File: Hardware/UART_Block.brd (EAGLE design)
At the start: 30.5 x 44.5 mm, 29 parts, among them U4 TPS62065

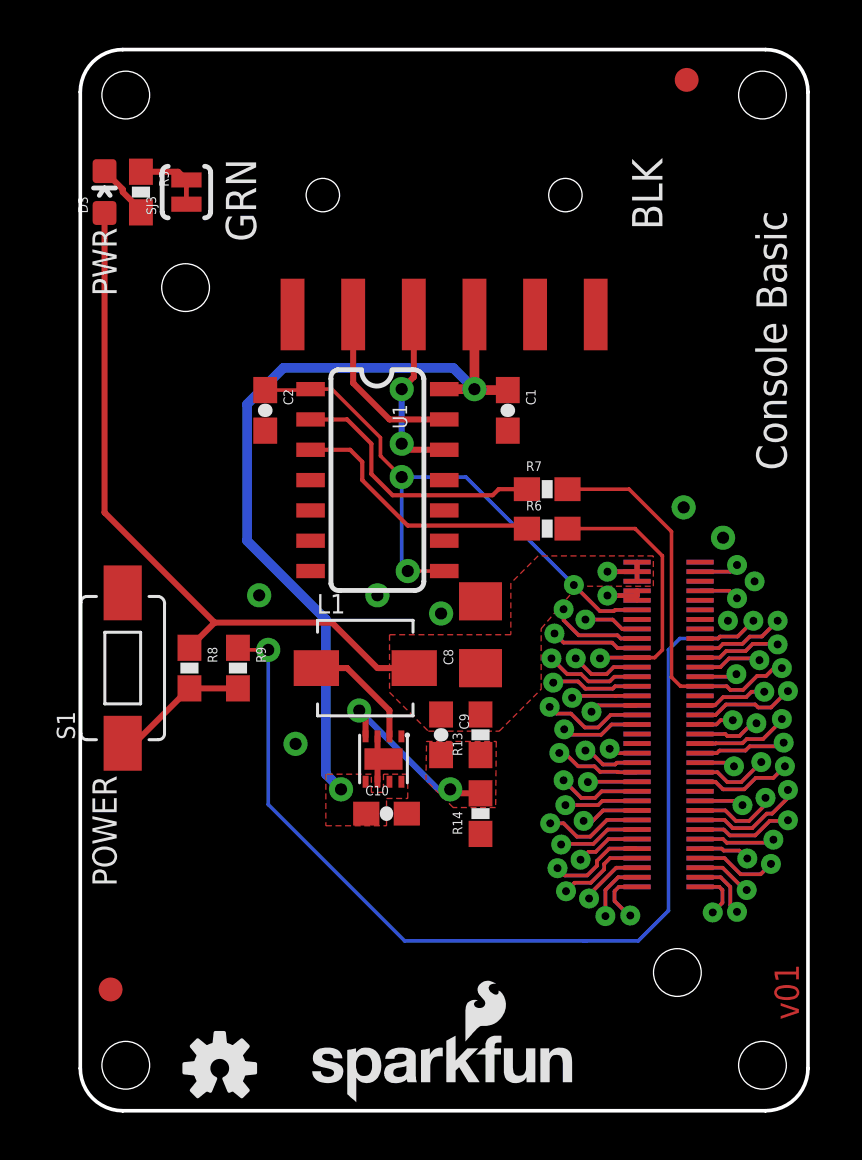
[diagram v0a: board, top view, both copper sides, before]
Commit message: added DCIN pin added DCIN enable circuit corrected Copper pours corrected name changed names of board and SCH replaced power button updated header footprint added units and cleaned up dimensions
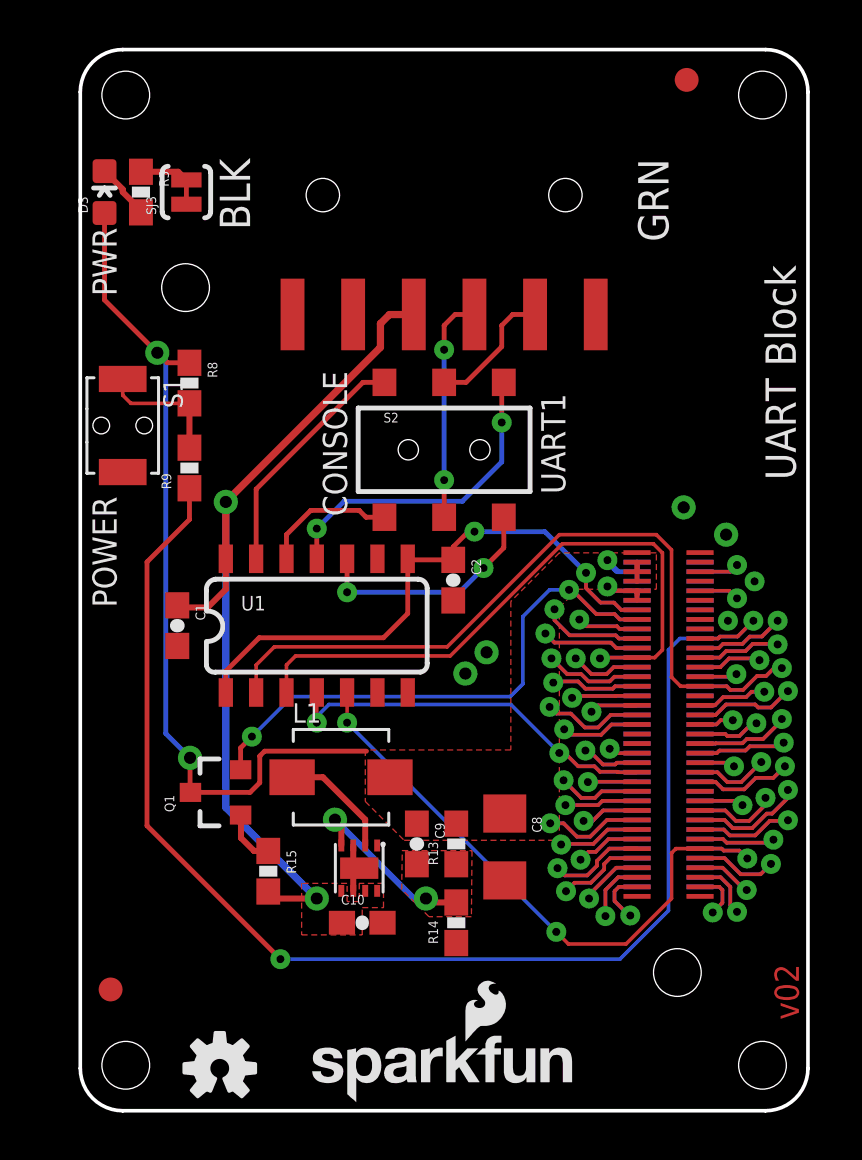
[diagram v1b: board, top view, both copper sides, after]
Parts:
- removed R6, R7: 100, SparkFun-Resistors:0603-RES
- added Q1: BSS138, SparkFun-DiscreteSemi:SOT23-3
- added R15: 1K, SparkFun-Resistors:0603-RES
- added S2: DPDT, SparkFun-Electromechanical:AYZ0202
- S1: device SparkFun-Electromechanical:TACTILE-SWITCH-1101NE -> SparkFun-Electromechanical:TACTILE_SWITCH-SMD-RIGHT-ANGLE
- moved C1 16.5 mm to (4.06, 20.3)
- moved R8 11.9 mm to (4.57, 30.5)
- moved C2 10.6 mm to (15.6, 22.2)
- moved S1 10.2 mm to (1.78, 28.7), turned to 270 degrees
- moved C8 8.95 mm to (17.8, 11.0), turned to 270 degrees
- moved R9 8.62 mm to (4.57, 26.9), turned to 90 degrees
- moved U1 6.60 mm to (9.91, 20.3), turned to 0 degrees
- moved L1 4.68 mm to (10.9, 14.0)
- moved C10 4.68 mm to (11.8, 7.87)
- moved R14 4.68 mm to (15.7, 7.87)
- moved C9 4.68 mm to (14.1, 11.2)
- moved R13 4.68 mm to (15.7, 11.2)
- moved U4 4.68 mm to (11.7, 10.2)
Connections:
- removed net N$3: R7.1, U1.2
- removed net N$4: R6.1, U1.3
- new net DCIN: E1.14, Q1.2, U$3.14
- new net N$1: Q1.1, R15.1
- new net UART1RX: S2.6, U1.10
- new net UART1TX: S2.3, U1.11
- new net UART2RX: S2.4, U1.12
- new net UART2TX: S2.1, U1.13
- net GND: now also JP2.5, JP2.6, S1.2; no longer JP2.1, JP2.2, S1.P$2
- net GP130_UART_1_RX: now also U1.5
- net GP131_UART_1_TX: now also U1.4
- net GP134_UART_2_RX: now also U1.3; no longer R6.2
- net GP135_UART_2_TX: now also U1.2; no longer R7.2
- net N$15: now also S1.1; no longer S1.P$1
- net RXD: now also JP2.2, S2.2; no longer JP2.5, U1.13
- net TXD: now also JP2.3, S2.5; no longer JP2.4, U1.12
- net VCC: now also JP2.4, R15.2; no longer JP2.3
- net VSYS: now also Q1.3
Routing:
- net DCIN: track 0.00 -> 25.8 mm, vias 0 -> 2
- net GP130_UART_1_RX: track 4.30 -> 27.0 mm, vias 1 -> 3
- net GP135_UART_2_TX: track 20.3 -> 35.5 mm
- net GP134_UART_2_RX: track 12.7 -> 27.6 mm
- net UART1TX: track 0.00 -> 13.5 mm, vias 0 -> 2
- net GP131_UART_1_TX: track 7.18 -> 19.9 mm, vias 1 -> 2
- net PWRBTN#: track 45.0 -> 57.4 mm
- net N$3: track 11.2 -> 0.00 mm
- net N$4: track 10.9 -> 0.00 mm
- net UART2TX: track 0.00 -> 10.1 mm
- net UART1RX: track 0.00 -> 10.0 mm, vias 0 -> 2
- net UART2RX: track 0.00 -> 5.65 mm
- net VSYS: track 34.2 -> 39.5 mm, vias 1 -> 3
- net VCC: track 34.3 -> 38.1 mm
- net N$1: track 0.00 -> 2.33 mm
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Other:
- board text added: "CONSOLE"
- board text added: "NOTE: Units are in Inches"
- board text added: "UART Block"
- board text added: "UART1"
- board text added: "v02"
- board text removed: "Connectors Go Here"
- board text removed: "Console Basic"
- board text removed: "LED's and selector switches go here"
- board text removed: "Max Board Length"
- board text removed: "Nothing goes here... I mean it."
- board text removed: "v01"

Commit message: Rev to 10, fix gnd, pwr, txt
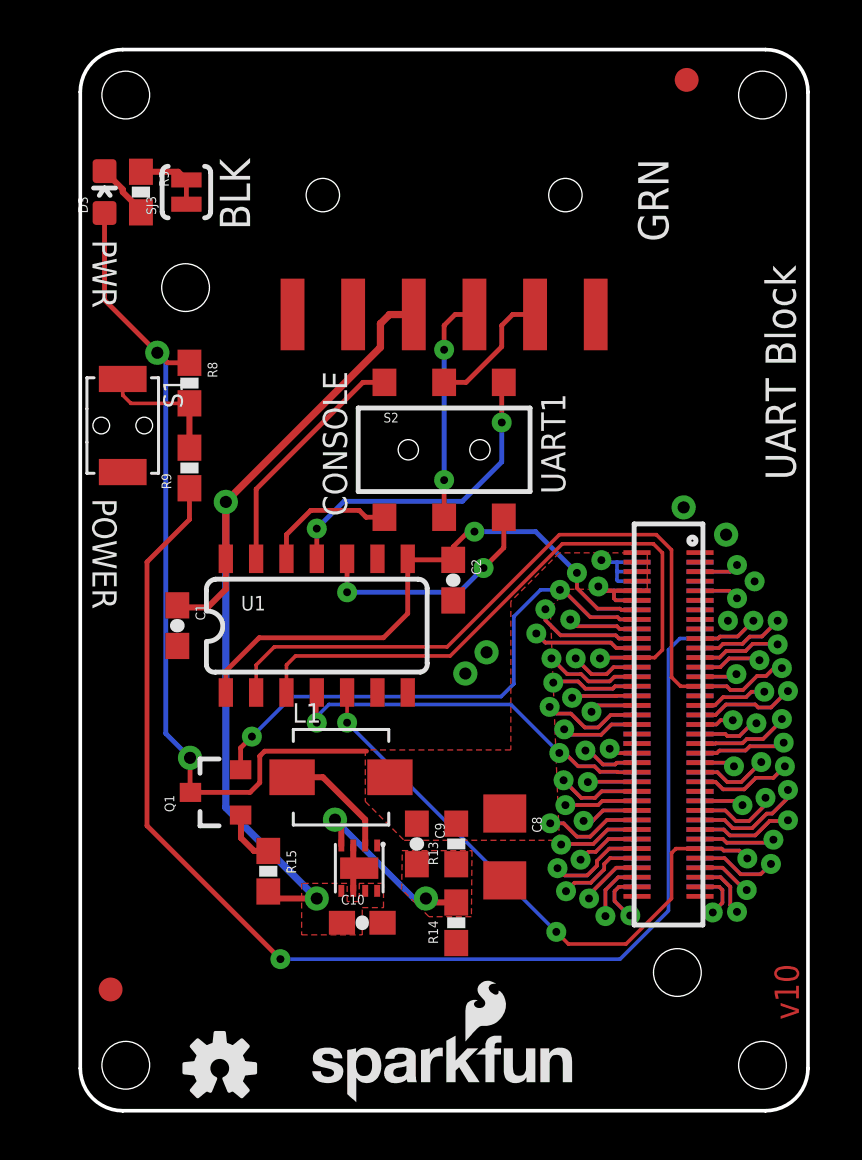
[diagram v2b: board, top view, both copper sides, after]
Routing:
- net 3.3V: track 3.63 -> 6.03 mm
- net USB_VBUS: track 8.18 -> 8.94 mm
- net USB_DN: track 8.47 -> 9.23 mm
- net USB_DP: track 5.16 -> 5.92 mm
- net VSYS: track 39.5 -> 40.0 mm
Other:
- board text added: "v10"
- board text removed: "v02"

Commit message: Fix packages, silk, filter cap.
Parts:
- C9: value 9.0pF -> 47pF
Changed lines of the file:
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@@
 <layer number="2" name="Route2" color="1" fill="3" visible="no" active="yes"/>
 <layer number="15" name="Route15" color="4" fill="6" visible="no" active="yes"/>
-<layer number="16" name="Bottom" color="1" fill="1" visible="yes" active="yes"/>
+<layer number="16" name="Bottom" color="1" fill="1" visible="no" active="yes"/>
 <layer number="17" name="Pads" color="2" fill="1" visible="yes" active="yes"/>
 <layer number="18" name="Vias" color="2" fill="1" visible="yes" active="yes"/>
@@
 <layer number="20" name="Dimension" color="15" fill="1" visible="yes" active="yes"/>
 <layer number="21" name="tPlace" color="16" fill="1" visible="yes" active="yes"/>
-<layer number="22" name="bPlace" color="14" fill="1" visible="yes" active="yes"/>
+<layer number="22" name="bPlace" color="14" fill="1" visible="no" active="yes"/>
 <layer number="23" name="tOrigins" color="15" fill="1" visible="yes" active="yes"/>
-<layer number="24" name="bOrigins" color="15" fill="1" visible="yes" active="yes"/>
+<layer number="24" name="bOrigins" color="15" fill="1" visible="no" active="yes"/>
 <layer number="25" name="tNames" color="7" fill="1" visible="no" active="yes"/>
 <layer number="26" name="bNames" color="7" fill="1" visible="no" active="yes"/>
@@
 <layer number="43" name="vRestrict" color="2" fill="10" visible="no" active="yes"/>
 <layer number="44" name="Drills" color="7" fill="1" visible="no" active="yes"/>
-<layer number="45" name="Holes" color="7" fill="1" visible="yes" active="yes"/>
+<layer number="45" name="Holes" color="7" fill="1" visible="no" active="yes"/>
 <layer number="46" name="Milling" color="3" fill="1" visible="no" active="yes"/>
-<layer number="51" name="tDocu" color="6" fill="1" visible="yes" active="yes"/>
+<layer number="51" name="tDocu" color="6" fill="1" visible="no" active="yes"/>
 <layer number="3" name="Route3" color="4" fill="3" visible="no" active="no"/>
 <layer number="4" name="Route4" color="1" fill="4" visible="no" active="no"/>
@@
 <text x="10.668" y="27.94" size="1.016" layer="21" font="vector" ratio="15" rot="R90" align="center">CONSOLE</text>
 <text x="19.812" y="27.94" size="1.016" layer="21" font="vector" ratio="15" rot="R90" align="center">UART1</text>
+<wire x1="12.192" y1="9.525" x2="12.192" y2="8.89" width="0.1524" layer="41"/>
 </plain>
 <attributes>
@@
 <element name="R13" library="SparkFun-Resistors" package="0603-RES" value="680k" x="15.748" y="11.176" rot="R90"/>
 <element name="R14" library="SparkFun-Resistors" package="0603-RES" value="120k" x="15.748" y="7.874" rot="R90"/>
-<element name="C9" library="SparkFun-Capacitors" package="0603-CAP" value="9.0pF" x="14.097" y="11.176" rot="R270">
-<attribute name="PROD_ID" value="CAP-09341" x="10.668" y="27.178" size="1.778" layer="27" rot="R270" display="off"/>
+<element name="C9" library="SparkFun-Capacitors" package="0603-CAP" value="47pF" x="14.097" y="11.176" rot="R270">
+<attribute name="PROD_ID" value="CAP-08913" x="10.668" y="27.178" size="1.778" layer="27" rot="R270" display="off"/>
 </element>
 <element name="C10" library="SparkFun-Capacitors" package="0603-CAP" value="4.7uF" x="11.811" y="7.874">

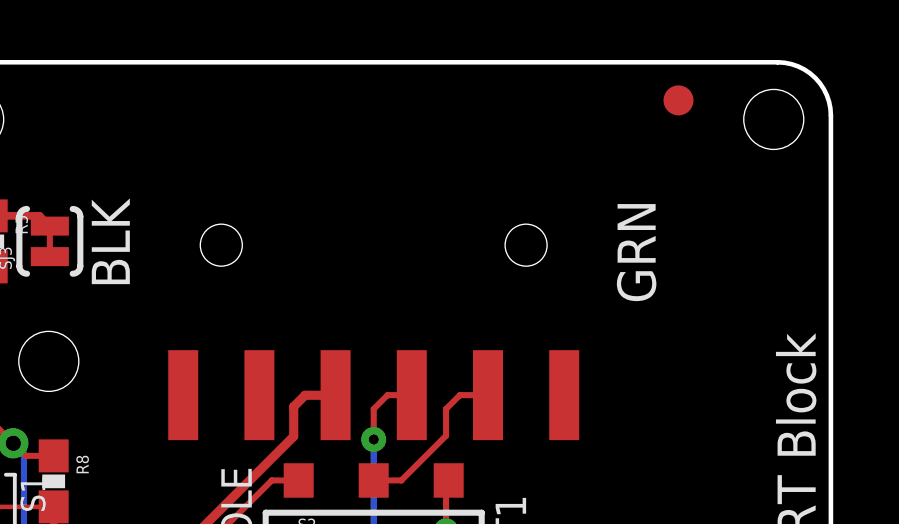
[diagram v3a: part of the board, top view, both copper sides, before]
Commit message: Ready for reds Updated and corrected some labels on UART connector. No signal changes. No known to-do items
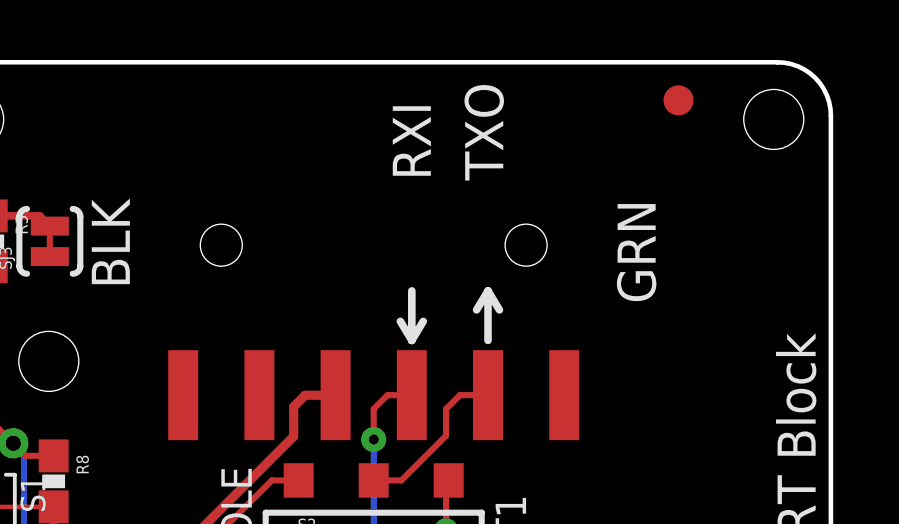
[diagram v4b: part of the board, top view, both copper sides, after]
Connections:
- net RXD renamed TXO
- net TXD renamed RXI
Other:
- board text added: "RXI"
- board text added: "TXO"
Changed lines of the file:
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@@
 <layer number="2" name="Route2" color="1" fill="3" visible="no" active="yes"/>
 <layer number="15" name="Route15" color="4" fill="6" visible="no" active="yes"/>
-<layer number="16" name="Bottom" color="1" fill="1" visible="no" active="yes"/>
+<layer number="16" name="Bottom" color="1" fill="1" visible="yes" active="yes"/>
 <layer number="17" name="Pads" color="2" fill="1" visible="yes" active="yes"/>
 <layer number="18" name="Vias" color="2" fill="1" visible="yes" active="yes"/>
@@
 <layer number="20" name="Dimension" color="15" fill="1" visible="yes" active="yes"/>
 <layer number="21" name="tPlace" color="16" fill="1" visible="yes" active="yes"/>
-<layer number="22" name="bPlace" color="14" fill="1" visible="no" active="yes"/>
+<layer number="22" name="bPlace" color="14" fill="1" visible="yes" active="yes"/>
 <layer number="23" name="tOrigins" color="15" fill="1" visible="yes" active="yes"/>
-<layer number="24" name="bOrigins" color="15" fill="1" visible="no" active="yes"/>
+<layer number="24" name="bOrigins" color="15" fill="1" visible="yes" active="yes"/>
 <layer number="25" name="tNames" color="7" fill="1" visible="no" active="yes"/>
 <layer number="26" name="bNames" color="7" fill="1" visible="no" active="yes"/>
@@
 <layer number="43" name="vRestrict" color="2" fill="10" visible="no" active="yes"/>
 <layer number="44" name="Drills" color="7" fill="1" visible="no" active="yes"/>
-<layer number="45" name="Holes" color="7" fill="1" visible="no" active="yes"/>
+<layer number="45" name="Holes" color="7" fill="1" visible="yes" active="yes"/>
 <layer number="46" name="Milling" color="3" fill="1" visible="no" active="yes"/>
-<layer number="51" name="tDocu" color="6" fill="1" visible="no" active="yes"/>
+<layer number="51" name="tDocu" color="6" fill="1" visible="yes" active="yes"/>
 <layer number="3" name="Route3" color="4" fill="3" visible="no" active="no"/>
 <layer number="4" name="Route4" color="1" fill="4" visible="no" active="no"/>
@@
 <text x="19.812" y="27.94" size="1.016" layer="21" font="vector" ratio="15" rot="R90" align="center">UART1</text>
 <wire x1="12.192" y1="9.525" x2="12.192" y2="8.89" width="0.1524" layer="41"/>
+<text x="17.145" y="40.513" size="1.27" layer="21" font="vector" ratio="15" rot="R90">RXI</text>
+<text x="19.558" y="40.513" size="1.27" layer="21" font="vector" ratio="15" rot="R90">TXO</text>
+<wire x1="19.05" y1="36.83" x2="19.05" y2="35.179" width="0.254" layer="21"/>
+<wire x1="19.05" y1="36.83" x2="18.669" y2="36.195" width="0.254" layer="21"/>
+<wire x1="19.05" y1="36.83" x2="19.431" y2="36.195" width="0.254" layer="21"/>
+<wire x1="16.51" y1="35.179" x2="16.51" y2="36.83" width="0.254" layer="21"/>
+<wire x1="16.51" y1="35.179" x2="16.891" y2="35.814" width="0.254" layer="21"/>
+<wire x1="16.51" y1="35.179" x2="16.129" y2="35.814" width="0.254" layer="21"/>
 </plain>
 <attributes>
@@
 <wire x1="10.16" y1="13.97" x2="8.872" y2="13.97" width="0.254" layer="1"/>
 </signal>
-<signal name="RXD">
+<signal name="TXO">
 <contactref element="JP2" pad="2"/>
 <contactref element="S2" pad="2"/>
@@
 <wire x1="18.114" y1="33.354" x2="19.05" y2="33.354" width="0.2032" layer="1"/>
 </signal>
-<signal name="TXD">
+<signal name="RXI">
 <contactref element="JP2" pad="3"/>
 <contactref element="S2" pad="5"/>
